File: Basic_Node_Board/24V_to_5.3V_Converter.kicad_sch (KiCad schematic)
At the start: 13 parts, among them J2 Conn_01x02, U1 TPS54560BQDDARQ1

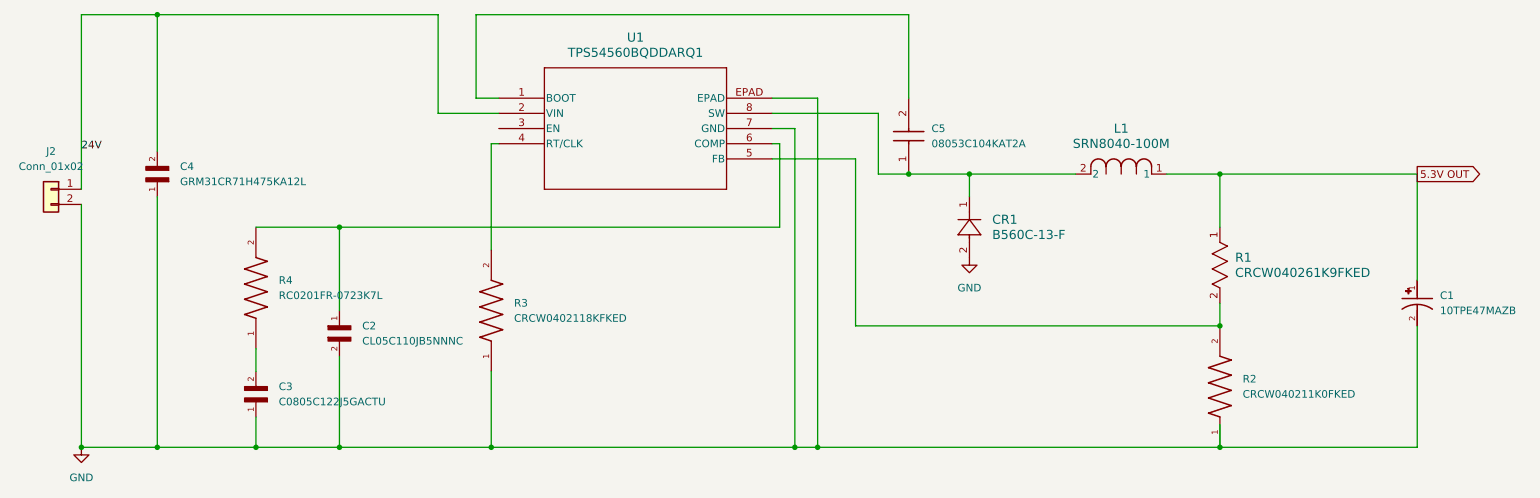
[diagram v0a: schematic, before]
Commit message: changed values for buck converter - Jacob K
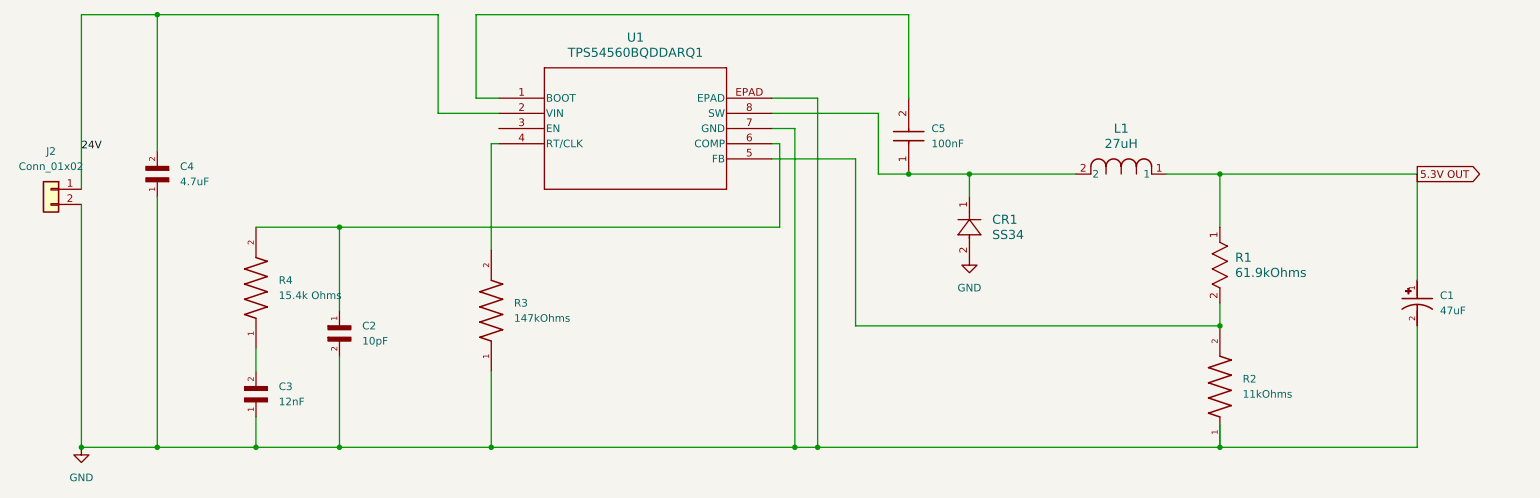
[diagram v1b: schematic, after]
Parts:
- C1: value 10TPE47MAZB -> 47uF
- C2: value CL05C110JB5NNNC -> 10pF
- C3: value C0805C122J5GACTU -> 12nF
- C4: value GRM31CR71H475KA12L -> 4.7uF
- C5: value 08053C104KAT2A -> 100nF
- CR1: value B560C-13-F -> SS34
- L1: value SRN8040-100M -> 27uH
- R1: value CRCW040261K9FKED -> 61.9kOhms
- R2: value CRCW040211K0FKED -> 11kOhms
- R3: value CRCW0402118KFKED -> 147kOhms
- R4: value RC0201FR-0723K7L -> 15.4k Ohms
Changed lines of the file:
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@@
 			)
 		)
-		(property "Value" "CRCW0402118KFKED"
+		(property "Value" "147kOhms"
 			(at 107.95 107.9499 90)
 			(effects
@@
 			)
 		)
-		(property "Value" "B560C-13-F"
+		(property "Value" "SS34"
 			(at 187.96 93.9799 90)
 			(effects
@@
 			)
 		)
-		(property "Value" "C0805C122J5GACTU"
+		(property "Value" "12nF"
 			(at 68.58 121.9199 90)
 			(effects
@@
 			)
 		)
-		(property "Value" "CL05C110JB5NNNC"
+		(property "Value" "10pF"
 			(at 82.55 111.7599 90)
 			(effects
@@
 			)
 		)
-		(property "Value" "RC0201FR-0723K7L"
+		(property "Value" "15.4k Ohms"
 			(at 68.58 104.1399 90)
 			(effects
@@
 			)
 		)
-		(property "Value" "GRM31CR71H475KA12L"
+		(property "Value" "4.7uF"
 			(at 52.07 85.0899 90)
 			(effects
@@
 			)
 		)
-		(property "Value" "CRCW040261K9FKED"
+		(property "Value" "61.9kOhms"
 			(at 228.6 100.3299 90)
 			(effects
@@
 			)
 		)
-		(property "Value" "SRN8040-100M"
+		(property "Value" "27uH"
 			(at 209.55 78.74 0)
 			(effects
@@
 			)
 		)
-		(property "Value" "10TPE47MAZB"
+		(property "Value" "47uF"
 			(at 262.89 106.6799 90)
 			(effects
@@
 			)
 		)
-		(property "Value" "08053C104KAT2A"
+		(property "Value" "100nF"
 			(at 177.8 78.7399 90)
 			(effects
@@
 			)
 		)
-		(property "Value" "CRCW040211K0FKED"
+		(property "Value" "11kOhms"
 			(at 229.87 120.6499 90)
 			(effects
